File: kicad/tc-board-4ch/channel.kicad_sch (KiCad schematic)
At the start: 19 parts, among them J101 DG127-5.08-02P, U101 MAX31855KASA+, U102 ISO7731DWR, U103 NCP1117ST33T3G

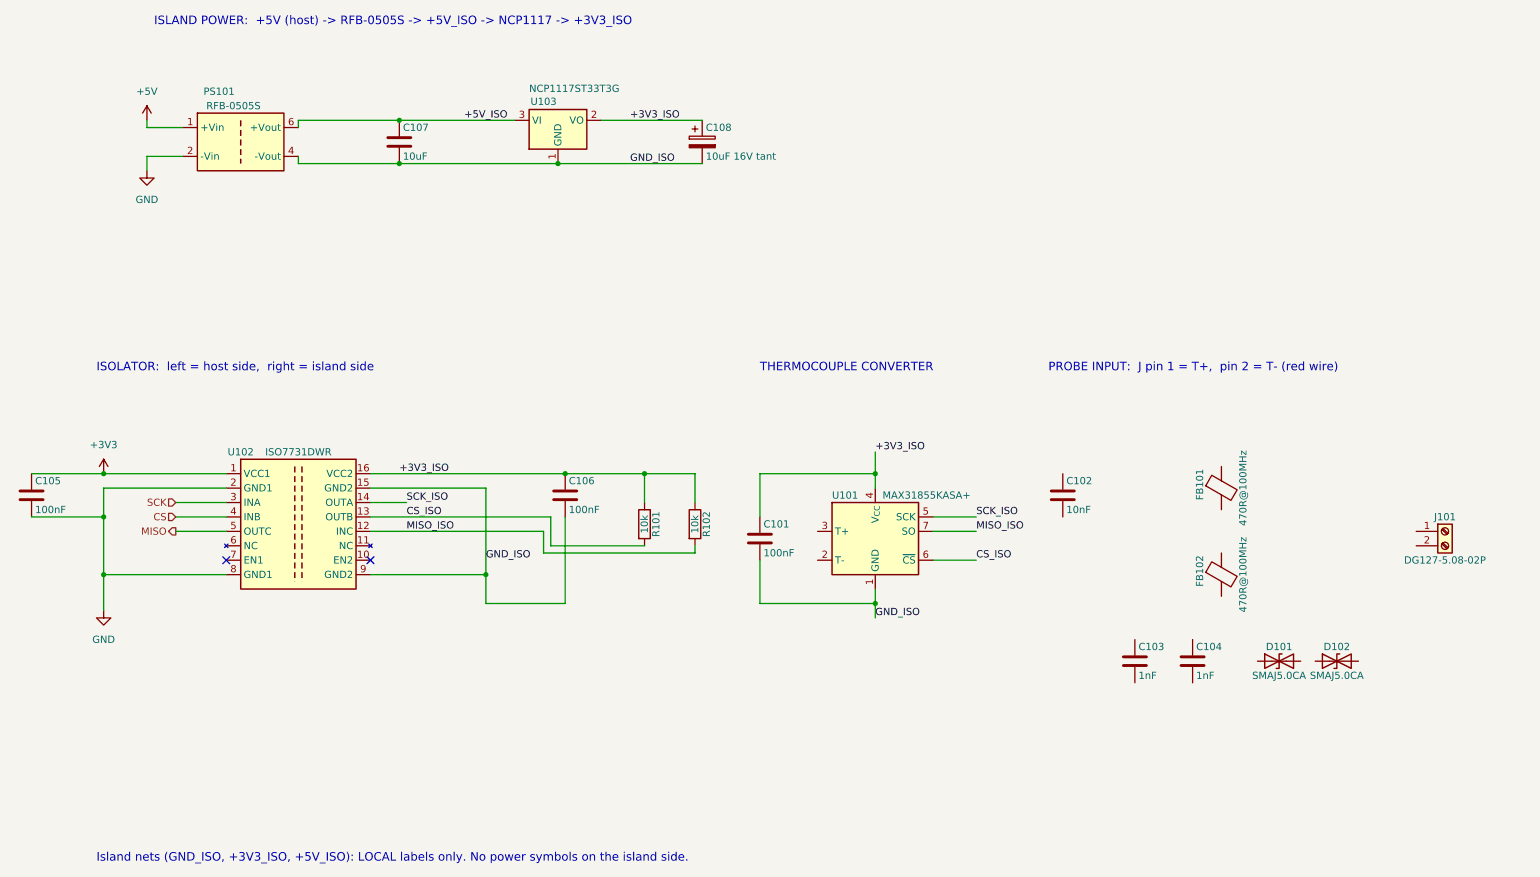
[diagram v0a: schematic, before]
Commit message: Schematic session 2: 4-channel isolated board ERC-clean
- Channel sheet: probe input chain (TVS, ferrite, 1 nF, 10 nF differential)
- Root sheet: sheet pins, host connector, 5V entry, SN74AHC125 MISO buffer,
  button connector, PWR_FLAGs
- ERC reports zero violations on all five sheets
- Roll the 2 Oct session into the archive; next step is the footprint check
  and PCB layout

Co-Authored-By: Claude Fable 5.1 <noreply@anthropic.com>
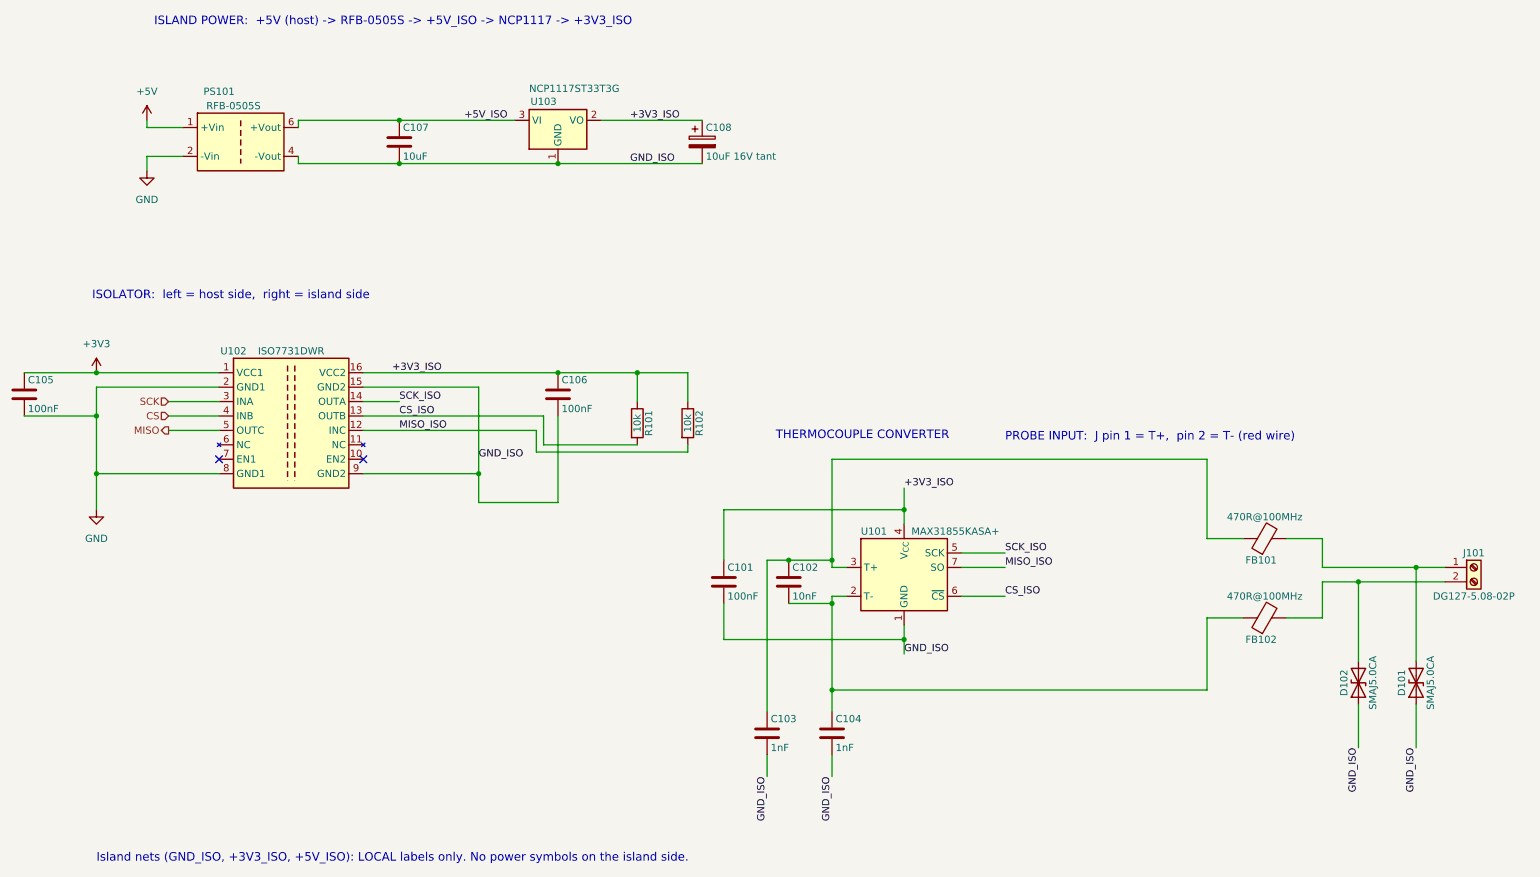
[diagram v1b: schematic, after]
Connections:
- net GND_ISO: now also C103.2, C104.2, D101.1 (A1), D102.1 (A1)
- net at C104.1: now also C102.2, FB102.1, U101.2 (T-)
- net at U101.3 (T+): now also C102.1, C103.1, FB101.1
- net at D101.2 (A2): now also FB101.2, J101.1 (Pin_1)
- net at D102.2 (A2): now also FB102.2, J101.2 (Pin_2)
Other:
- moved on the sheet: C101, C102, C103, C104, C105, C106, D101, D102, FB101, FB102, J101, R101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

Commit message: Pre-layout session: footprints verified, DG127 footprint added, chassis network dropped
- Confirm the Traco TMA footprint matches the RFB-0505S drawing so the DC-DC
  pads can be trusted; JST PH, header, tantalum, TVS and ferrite also pass
- Add a true-outline Degson DG127 screw-terminal footprint and box 3D model
  because the Phoenix stand-in drew the body 4 mm too deep for edge placement
- Track the project's own hand-written 3D models despite the vendor-model ignore
- Leave the chassis network out: grounded-junction probes already reference
  each island, so the jumper could never be closed; caveat recorded for
  insulated probes in a future revision

Co-Authored-By: Claude Fable 5.1 <noreply@anthropic.com>
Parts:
- J101: footprint Connector_Phoenix_MSTB:PhoenixContact_MSTBA_2,5_2-G-5,08_1x02_P5.08mm_Horizontal -> milk-depot:Degson_DG127-5.08-02P_1x02_P5.08mm_Horizontal
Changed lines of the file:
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@@
 			)
 		)
-		(property "Footprint" "Connector_Phoenix_MSTB:PhoenixContact_MSTBA_2,5_2-G-5,08_1x02_P5.08mm_Horizontal"
+		(property "Footprint" "milk-depot:Degson_DG127-5.08-02P_1x02_P5.08mm_Horizontal"
 			(at 273.05 120.65 0)
 			(hide yes)
